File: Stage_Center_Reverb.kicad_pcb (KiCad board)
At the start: 2 copper layers, 75 x 50 mm, 43 parts, among them J10 Power, J2 Output, J3 Tank, SW2 kill, U1 TL072, U10 L78L15, U11 L79L15, U2 TL072

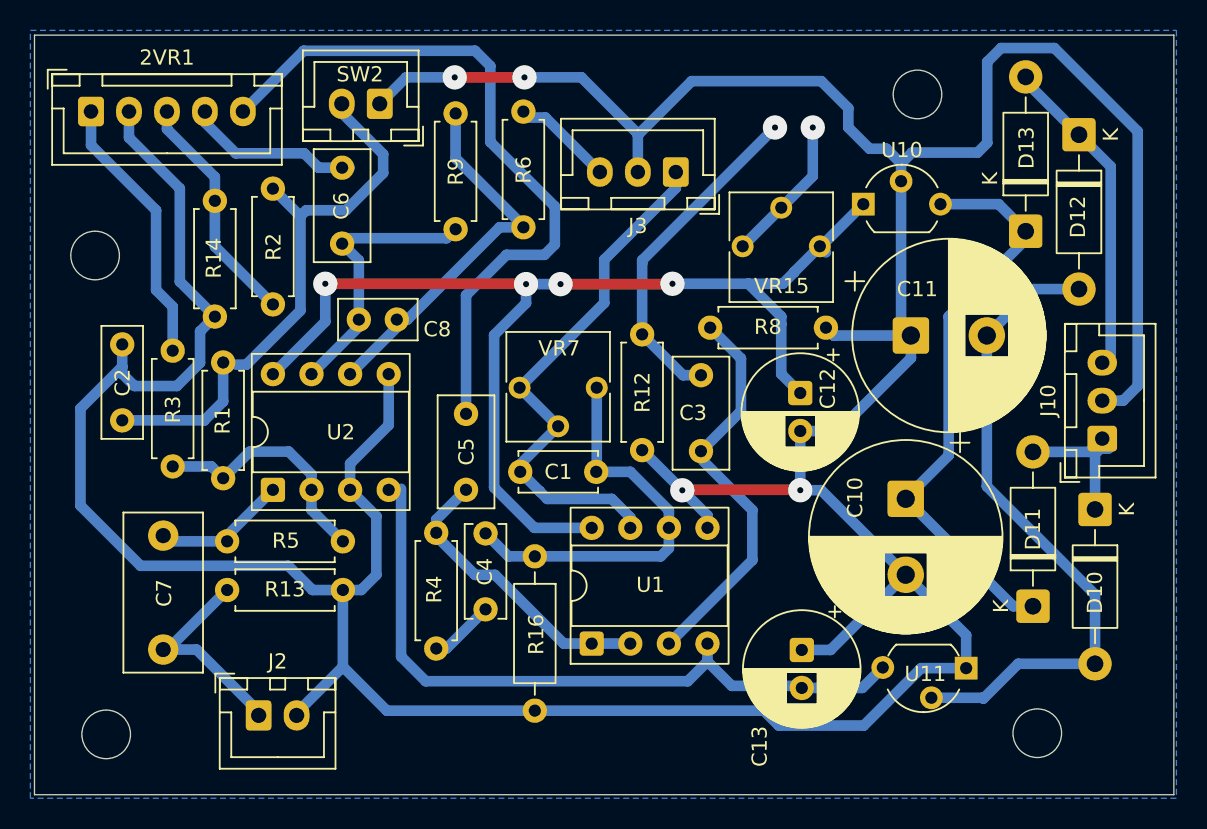
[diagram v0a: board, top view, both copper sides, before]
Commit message: ICまわりの配置を修正
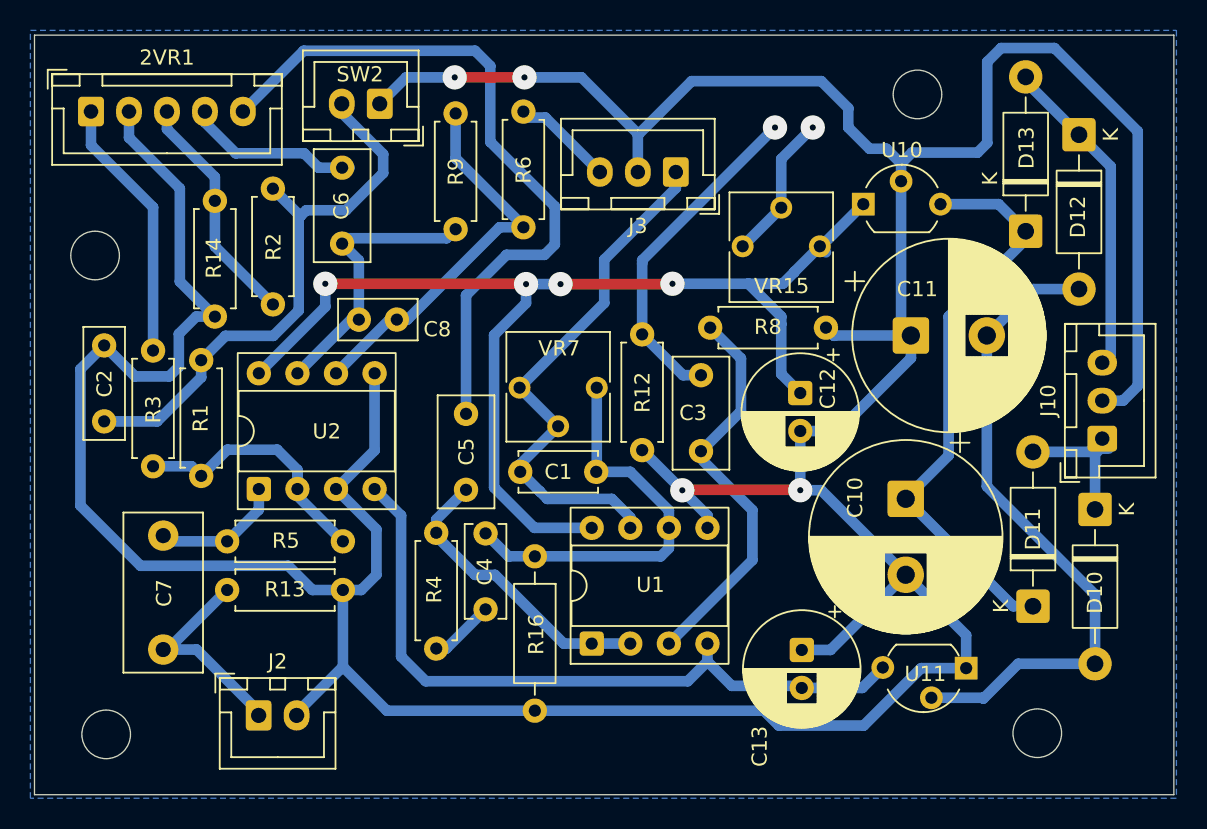
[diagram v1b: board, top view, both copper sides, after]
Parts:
- moved R1 1.45 mm to (104.5, 105.5)
- moved R3 1.29 mm to (101.3, 104.9)
- moved C2 1.19 mm to (98.1, 101.9)
- moved U2 0.93 mm to (108.3, 106.3)
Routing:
- net Net-(U2A--): track 16.1 -> 18.0 mm
- net Net-(SW2-B): track 36.8 -> 37.9 mm
- net GNDPWR: track 290.2 -> 291.3 mm
- net Net-(C6-Pad1): track 18.2 -> 19.3 mm
- net -15V: track 46.4 -> 47.1 mm
- net Net-(U2B--): track 25.1 -> 25.7 mm
- net Net-(2VR1-Pad2): track 18.0 -> 17.4 mm

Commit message: 線が近いところを修正、ハッチングを45°に変更してみた
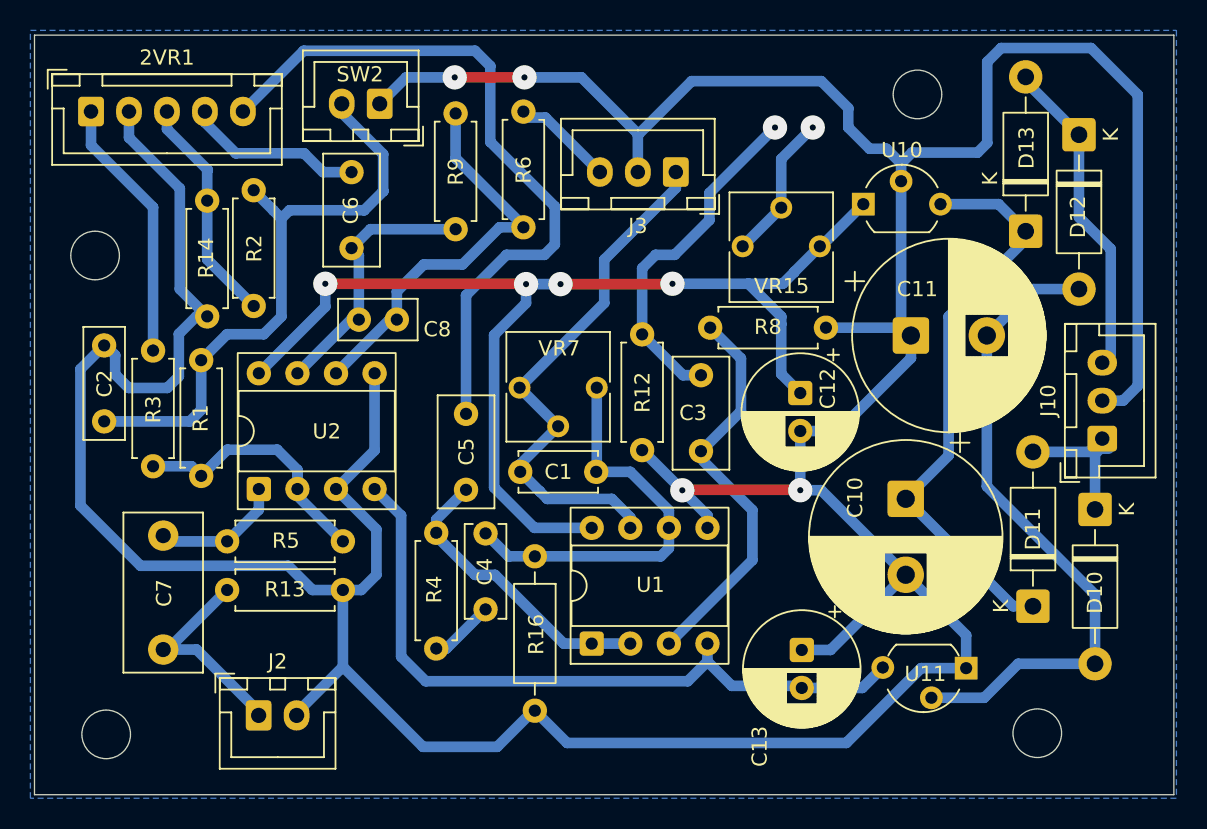
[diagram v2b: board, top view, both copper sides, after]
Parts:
- moved R2 1.27 mm to (107.9, 86.7)
- moved C6 0.69 mm to (114.4, 90.5)
- moved R14 0.51 mm to (104.9, 87.4)
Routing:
- net GNDPWR: track 291.3 -> 295.9 mm
- net Net-(SW2-B): track 37.9 -> 39.9 mm
- net Net-(C6-Pad1): track 19.3 -> 18.2 mm
- net Net-(U2B--): track 25.7 -> 26.7 mm
- net Net-(SW1a1-B): track 22.2 -> 23.0 mm
- net +15V: track 76.4 -> 75.8 mm

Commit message: GNDはベタだけにする
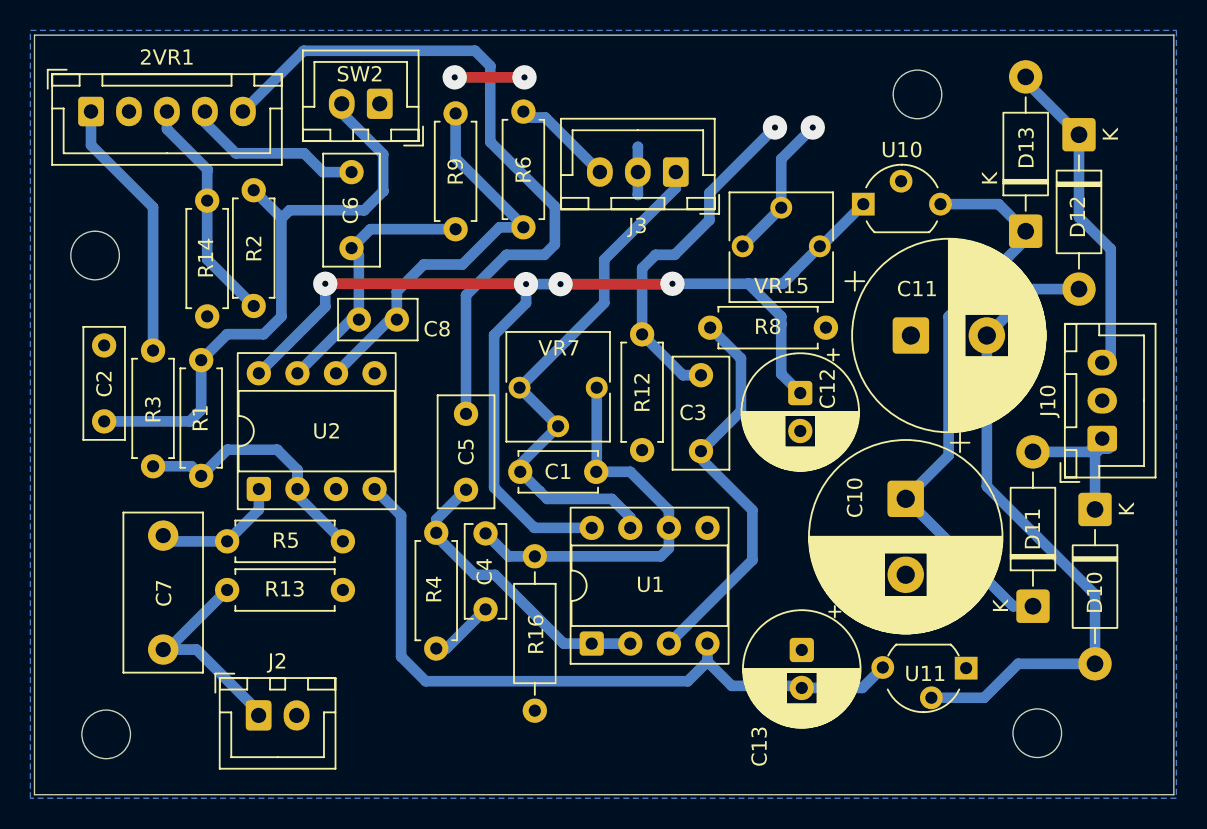
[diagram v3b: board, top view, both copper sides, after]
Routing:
- net GNDPWR: track 295.9 -> 10.5 mm, vias 4 -> 2

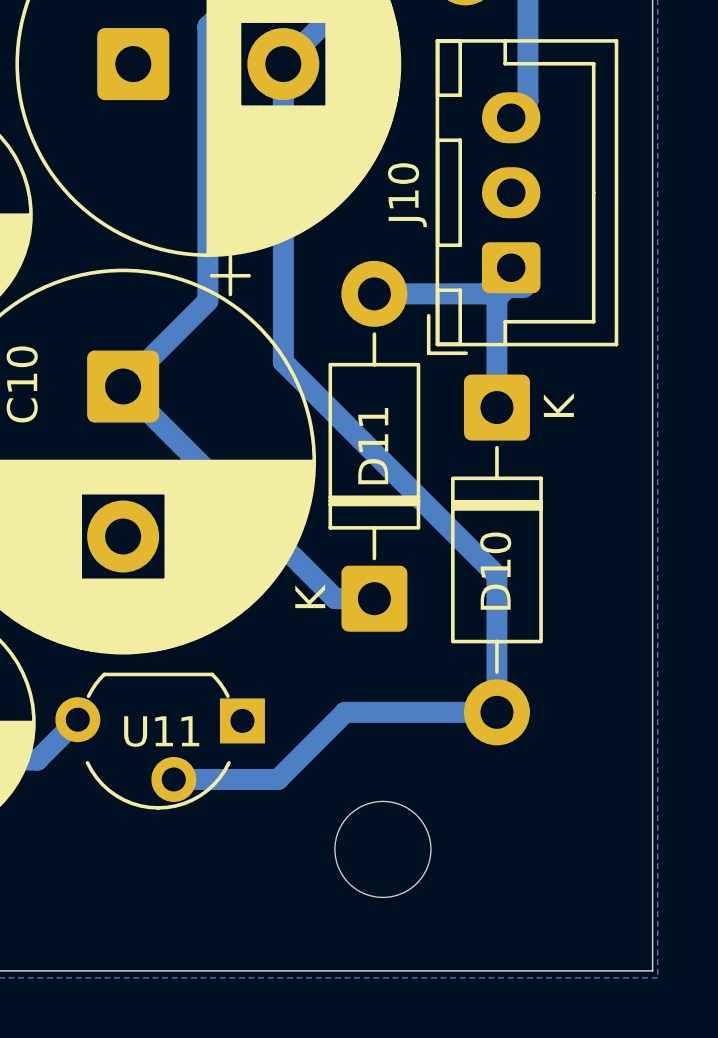
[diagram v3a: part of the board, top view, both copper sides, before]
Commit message: GNDベタ禁止エリアを追加
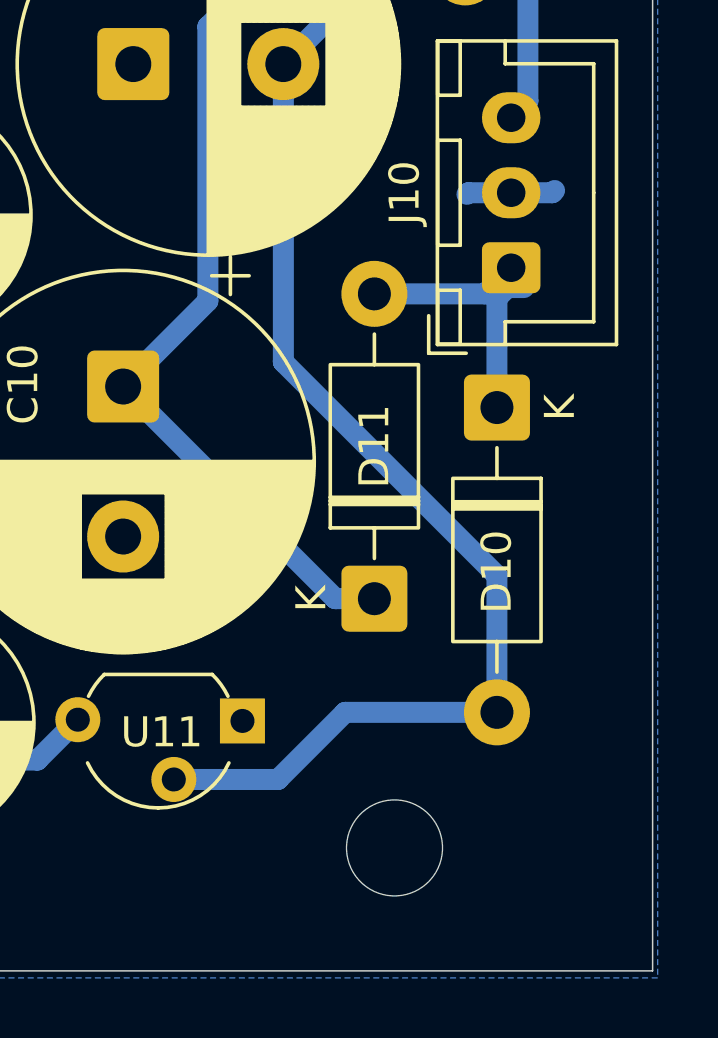
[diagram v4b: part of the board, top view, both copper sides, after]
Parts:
- moved H4 0.39 mm to (159.9, 122.4)
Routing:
- net GNDPWR: track 10.5 -> 13.5 mm

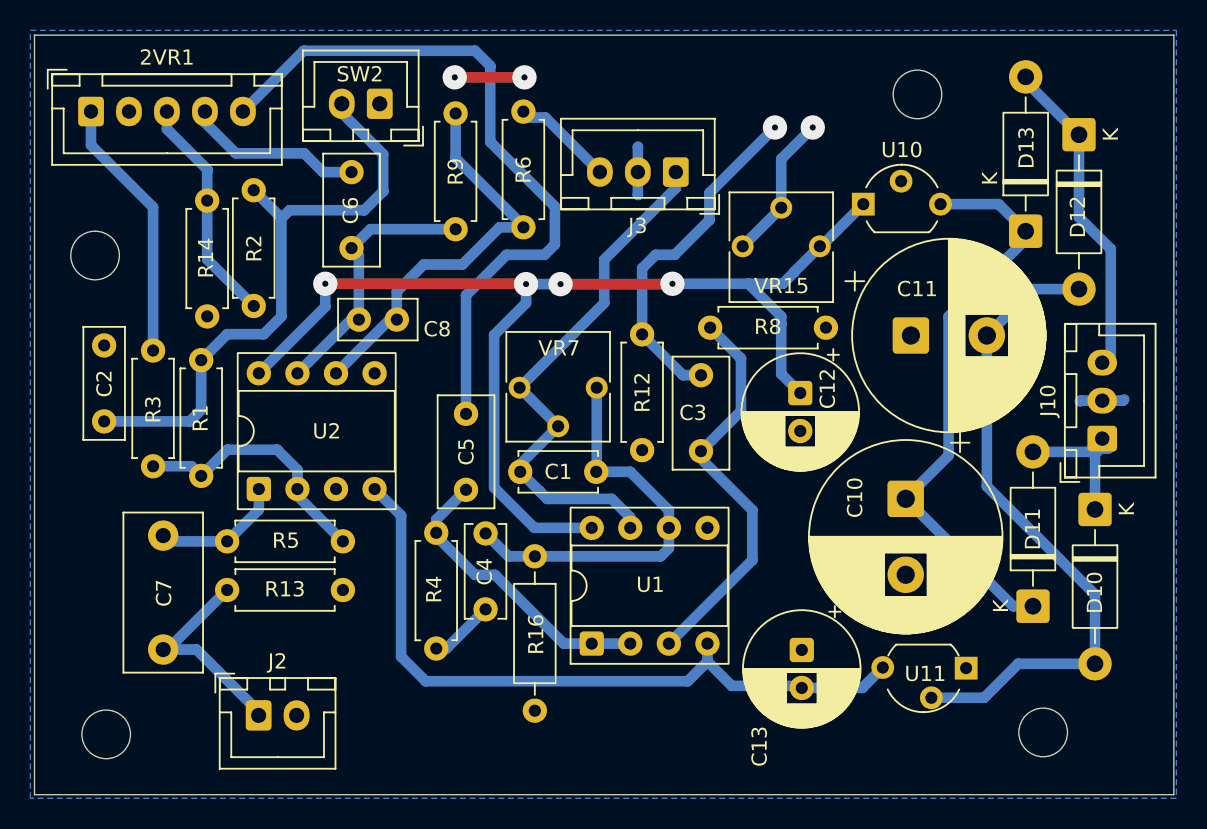
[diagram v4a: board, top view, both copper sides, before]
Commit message: 配線を修正
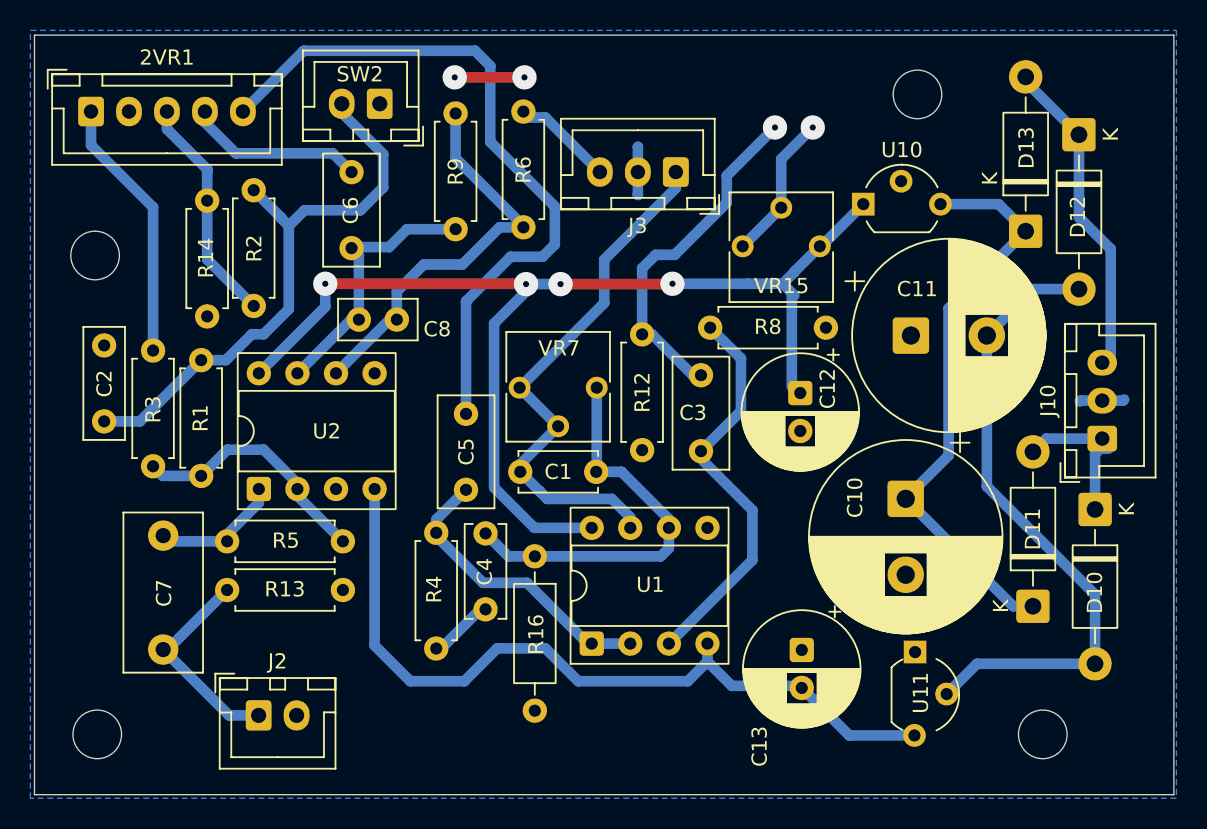
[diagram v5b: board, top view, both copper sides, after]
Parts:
- moved U11 3.00 mm to (151.8, 117.3), turned to -90 degrees
- moved H3 0.59 mm to (97.6, 122.5)
- moved H4 0.13 mm to (159.9, 122.5)
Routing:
- net -15V: track 47.1 -> 52.3 mm
- net Net-(SW2-B): track 39.9 -> 37.9 mm
- net Net-(U2A--): track 18.0 -> 16.5 mm
- net +15V: track 75.8 -> 74.3 mm
- net Net-(D10-A): track 43.6 -> 42.5 mm
- net Net-(D11-K): track 38.5 -> 39.1 mm

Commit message: 配置を修正
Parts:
- moved C8 0.32 mm to (117.3, 94.9)
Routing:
- net Net-(SW1a1-B): track 23.0 -> 23.8 mm
- net Net-(U2A--): track 16.5 -> 17.3 mm
- net Net-(U2B--): track 26.7 -> 25.9 mm
- net Net-(U1A-+): track 25.7 -> 26.4 mm
